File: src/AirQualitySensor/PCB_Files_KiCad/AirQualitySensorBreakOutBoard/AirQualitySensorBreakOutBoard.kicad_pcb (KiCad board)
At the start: 2 copper layers, 36 x 113.8 mm, 23 parts, among them J1 Conn_01x02_Male, J2 Conn_01x02_Male, J3 Conn_01x02_Male, J4 Conn_01x07_Male, Q1 IRLB8721PBF, U1 PMS5003, U2 PMS5003, U3 SPS30, U4 SHT31, U6 lilygo-ttgo-t-sim7000g-esp32-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, U7 Buck/Boost_Converter

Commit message: updated version
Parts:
- removed U7: Buck/Boost_Converter, Surfside Science:Buck_Boost_Converter
- added REF**: Buck_Boost_Converter, Surfside Science:Buck_Boost_Converter, F.Cu at (87.3, 38.8)
- moved ? 221.9 mm to (18.4, 17.9), turned to 90 degrees
- moved R4 210.4 mm to (25.6, 22.4), turned to 0 degrees
- moved R3 206.7 mm to (33.1, 19.6), turned to 180 degrees
- moved R2 206.4 mm to (18.6, 32.9), turned to 90 degrees
- moved U4 198.2 mm to (32.6, 27.8), turned to 0 degrees
- moved REF** 194.8 mm to (17.9, 45.9), turned to 90 degrees
- moved U1 194.8 mm to (26.8, 36.3), turned to 0 degrees
- moved U3 192.4 mm to (34.5, 31.5), turned to 180 degrees
- moved J4 187.9 mm to (55.1, 20.5), turned to -90 degrees
- moved C2 185.6 mm to (44.1, 29.9), turned to 0 degrees
- moved Q1 178.4 mm to (52.5, 30.2), turned to 0 degrees
- moved U2 169.9 mm to (54.9, 35.8), turned to 0 degrees
- moved J2 168.7 mm to (93.7, 18.9), turned to -90 degrees
- moved C1 167.1 mm to (67.6, 30.4), turned to 90 degrees
- moved U6 166.8 mm to (63.1, 33.1), turned to 90 degrees
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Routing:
- net PULLUP_1: track 70.8 -> 68.4 mm
- net GND: track 230.3 -> 232.0 mm
- net 3V3: track 144.4 -> 143.6 mm
- net VDD2: track 159.0 -> 159.7 mm
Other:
- board size 36 x 113.8 mm -> 113.8 x 36 mm

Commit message: Fixed bug aqs
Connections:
- U6 pad 12: unconnected-(U6-Pad12) -> VDD_EN
- U6 pad 13: VDD_EN -> unconnected-(U6-Pad13)
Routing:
- net VDD_EN: track 34.6 -> 31.9 mm
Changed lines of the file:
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@@
   (net 7 "unconnected-(U6-Pad03)")
   (net 8 "unconnected-(U6-Pad04)")
-  (net 9 "unconnected-(U6-Pad12)")
+  (net 9 "unconnected-(U6-Pad13)")
   (net 10 "unconnected-(U6-Pad14)")
   (net 11 "unconnected-(U6-Pad15)")
@@
       (net 34 "SPI_SS") (pinfunction "SPI__SS") (pintype "input"))
     (pad "12" thru_hole circle (at -14.12 -4.6 90) (size 2 2) (drill 1.02) (layers *.Cu *.Mask)
-      (net 9 "unconnected-(U6-Pad12)") (pinfunction "12") (pintype "input"))
+      (net 38 "VDD_EN") (pinfunction "12") (pintype "input"))
     (pad "13" thru_hole circle (at -14.12 -7.14 90) (size 2 2) (drill 1.02) (layers *.Cu *.Mask)
-      (net 38 "VDD_EN") (pinfunction "13") (pintype "input"))
+      (net 9 "unconnected-(U6-Pad13)") (pinfunction "13") (pintype "input"))
     (pad "14" thru_hole circle (at -14.12 -9.68 90) (size 2 2) (drill 1.02) (layers *.Cu *.Mask)
       (net 10 "unconnected-(U6-Pad14)") (pinfunction "14") (pintype "input"))
@@
   (segment (start 39.86 20.5) (end 38.085 18.725) (width 1) (layer "F.Cu") (net 37))
   (segment (start 38.085 18.725) (end 38.085 16.663353) (width 1) (layer "F.Cu") (net 37))
-  (segment (start 62.5 33.51) (end 62.5 33.6) (width 1) (layer "F.Cu") (net 38))
+  (segment (start 71.6 43.8) (end 70.174649 45.225351) (width 1) (layer "F.Cu") (net 38))
+  (segment (start 62.5 33.6) (end 65.6 36.7) (width 1) (layer "F.Cu") (net 38))
   (segment (start 71.6 38.8) (end 71.6 43.8) (width 1) (layer "F.Cu") (net 38))
-  (segment (start 69.5 36.7) (end 71.6 38.8) (width 1) (layer "F.Cu") (net 38))
-  (segment (start 70.174649 45.225351) (end 55.974649 45.225351) (width 1) (layer "F.Cu") (net 38))
   (segment (start 65.6 36.7) (end 69.5 36.7) (width 1) (layer "F.Cu") (net 38))
-  (segment (start 55.974649 45.225351) (end 55.974649 47.243002) (width 1) (layer "F.Cu") (net 38))
-  (segment (start 62.5 33.6) (end 65.6 36.7) (width 1) (layer "F.Cu") (net 38))
-  (segment (start 71.6 43.8) (end 70.174649 45.225351) (width 1) (layer "F.Cu") (net 38))
+  (segment (start 62.5 33.51) (end 62.5 33.6) (width 1) (layer "F.Cu") (net 38))
+  (segment (start 69.5 36.7) (end 71.6 38.8) (width 1) (layer "F.Cu") (net 38))
+  (segment (start 58.514649 45.485351) (end 58.514649 47.243002) (width 1) (layer "F.Cu") (net 38))
+  (segment (start 58.774649 45.225351) (end 58.514649 45.485351) (width 1) (layer "F.Cu") (net 38))
+  (segment (start 70.174649 45.225351) (end 58.774649 45.225351) (width 1) (layer "F.Cu") (net 38))
 )

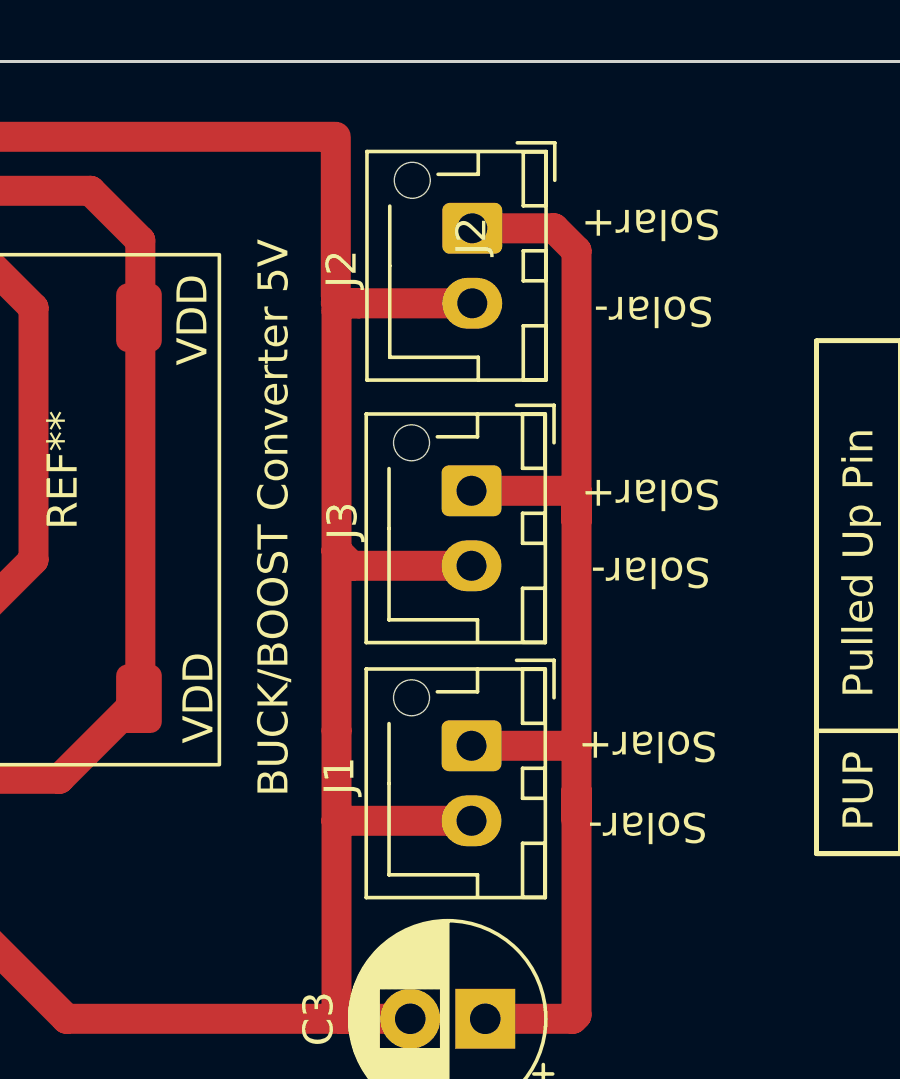
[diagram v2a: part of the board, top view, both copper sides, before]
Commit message: Updated AQS sensor code
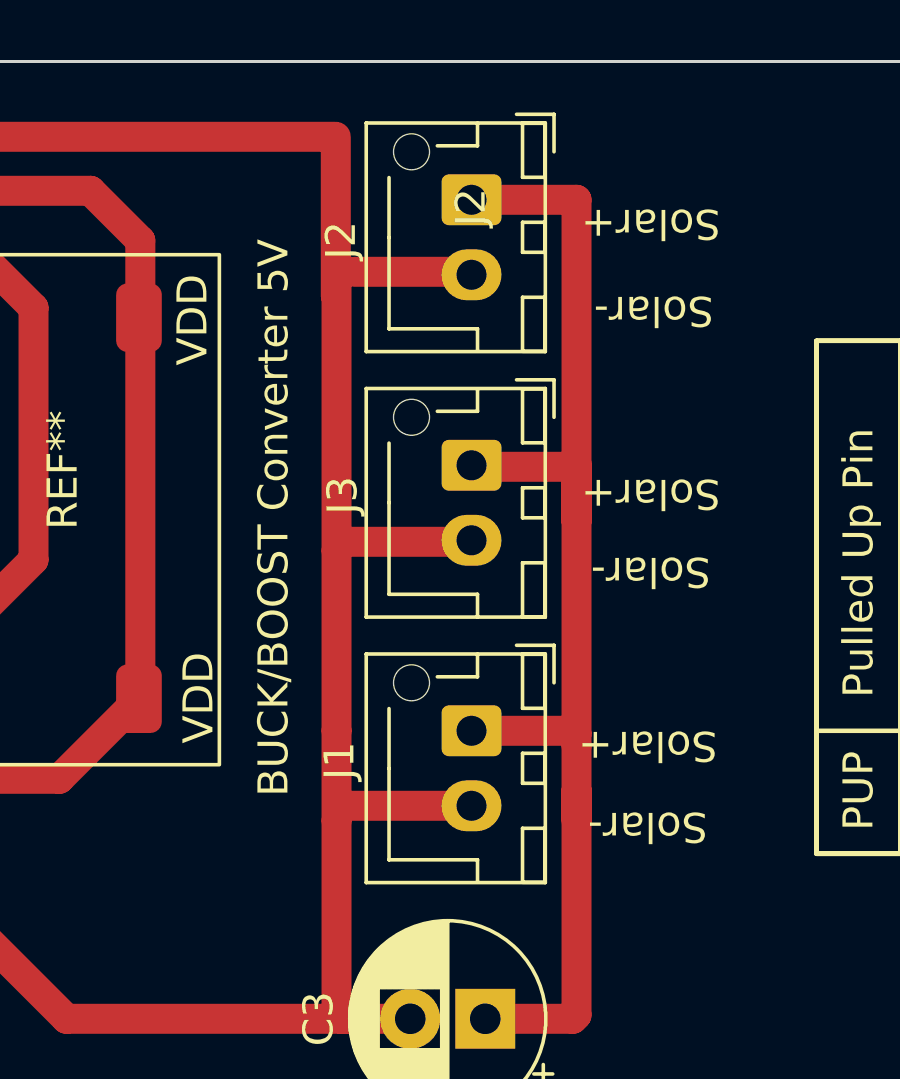
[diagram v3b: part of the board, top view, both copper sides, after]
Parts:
- moved J2 0.95 mm to (93.7, 18.0)
- moved J3 0.85 mm to (93.7, 26.9)
- moved J1 0.50 mm to (93.7, 35.7)
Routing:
- net Solar_IN: track 41.5 -> 43.6 mm
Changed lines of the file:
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@@
   (net 38 "VDD_EN")
   (footprint "Connector_JST:JST_XH_B2B-XH-AM_1x02_P2.50mm_Vertical" (layer "F.Cu")
-    (at 93.725 18.95 -90)
+    (at 93.7 18 -90)
     (descr "JST XH series connector, B2B-XH-AM, with boss (http://www.jst-mfg.com/product/pdf/eng/eXH.pdf), generated with kicad-footprint-generator")
     (tags "connector JST XH vertical boss")
@@
   )
   (footprint "Connector_JST:JST_XH_B2B-XH-AM_1x02_P2.50mm_Vertical" (layer "F.Cu")
-    (at 93.7 36.2 -90)
+    (at 93.7 35.7 -90)
     (descr "JST XH series connector, B2B-XH-AM, with boss (http://www.jst-mfg.com/product/pdf/eng/eXH.pdf), generated with kicad-footprint-generator")
     (tags "connector JST XH vertical boss")
@@
   )
   (footprint "Connector_JST:JST_XH_B2B-XH-AM_1x02_P2.50mm_Vertical" (layer "F.Cu")
-    (at 93.7 27.7 -90)
+    (at 93.7 26.85 -90)
     (descr "JST XH series connector, B2B-XH-AM, with boss (http://www.jst-mfg.com/product/pdf/eng/eXH.pdf), generated with kicad-footprint-generator")
     (tags "connector JST XH vertical boss")
@@
   (segment (start 57.357621 27.882379) (end 55.04 30.2) (width 1) (layer "F.Cu") (net 2))
   (segment (start 25.494649 47.243002) (end 27.537651 45.2) (width 1) (layer "F.Cu") (net 3))
+  (segment (start 93.65 29.4) (end 89.3 29.4) (width 1) (layer "F.Cu") (net 3))
   (segment (start 73.5 14.5) (end 74.9 15.9) (width 1) (layer "F.Cu") (net 3))
   (segment (start 69.4 38.4) (end 62.8 38.4) (width 1) (layer "F.Cu") (net 3))
   (segment (start 69.5 43.7) (end 70.2 43) (width 1) (layer "F.Cu") (net 3))
   (segment (start 44.9 43.7) (end 46.8 43.7) (width 1) (layer "F.Cu") (net 3))
-  (segment (start 93.7 38.7) (end 89.2 38.7) (width 1) (layer "F.Cu") (net 3))
+  (segment (start 93.7 38.35) (end 93.7 38.2) (width 1) (layer "F.Cu") (net 3))
   (segment (start 89.2 35.7) (end 89.2 29.7) (width 1) (layer "F.Cu") (net 3))
+  (segment (start 89.2 29.7) (end 89.2 20) (width 1) (layer "F.Cu") (net 3))
   (segment (start 89.2 38.7) (end 89.2 35.7) (width 1) (layer "F.Cu") (net 3))
-  (segment (start 93.7 30.2) (end 89.7 30.2) (width 1) (layer "F.Cu") (net 3))
   (segment (start 89.2 45.125) (end 89.2 38.7) (width 1) (layer "F.Cu") (net 3))
   (segment (start 46.8 43.7) (end 69.5 43.7) (width 1) (layer "F.Cu") (net 3))
+  (segment (start 89.8 20.4) (end 93.6 20.4) (width 1) (layer "F.Cu") (net 3))
   (segment (start 89.5 45.3) (end 80.2 45.3) (width 1) (layer "F.Cu") (net 3))
   (segment (start 27.537651 45.2) (end 43.4 45.2) (width 1) (layer "F.Cu") (net 3))
-  (segment (start 89.2 21.7) (end 89.45 21.45) (width 1) (layer "F.Cu") (net 3))
+  (segment (start 93.7 29.35) (end 93.65 29.4) (width 1) (layer "F.Cu") (net 3))
   (segment (start 46.617621 43.517621) (end 46.8 43.7) (width 1) (layer "F.Cu") (net 3))
   (segment (start 91.65738 45.3) (end 89.375 45.3) (width 1) (layer "F.Cu") (net 3))
@@
   (segment (start 58.394649 14.605351) (end 58.5 14.5) (width 1) (layer "F.Cu") (net 3))
   (segment (start 70.2 39.2) (end 69.4 38.4) (width 1) (layer "F.Cu") (net 3))
-  (segment (start 89.45 21.45) (end 89.95 21.45) (width 1) (layer "F.Cu") (net 3))
-  (segment (start 89.2 29.7) (end 89.2 21.7) (width 1) (layer "F.Cu") (net 3))
+  (segment (start 93.6 20.4) (end 93.7 20.5) (width 1) (layer "F.Cu") (net 3))
   (segment (start 66.8 35) (end 62 30.2) (width 1) (layer "F.Cu") (net 3))
-  (segment (start 89.95 21.45) (end 89.175 21.45) (width 1) (layer "F.Cu") (net 3))
   (segment (start 91.85738 45.2) (end 91.75738 45.3) (width 1) (layer "F.Cu") (net 3))
   (segment (start 70.2 43) (end 70.2 39.2) (width 1) (layer "F.Cu") (net 3))
   (segment (start 80.2 45.3) (end 69.9 35) (width 1) (layer "F.Cu") (net 3))
   (segment (start 69.9 35) (end 66.8 35) (width 1) (layer "F.Cu") (net 3))
-  (segment (start 89.7 30.2) (end 89.2 29.7) (width 1) (layer "F.Cu") (net 3))
   (segment (start 89.175 21.2) (end 89.175 15.9) (width 1) (layer "F.Cu") (net 3))
   (segment (start 58.394649 16.653002) (end 58.394649 14.605351) (width 1) (layer "F.Cu") (net 3))
-  (segment (start 93.792621 21.517621) (end 93.725 21.45) (width 1) (layer "F.Cu") (net 3))
   (segment (start 57.58 33.18) (end 57.58 30.2) (width 1) (layer "F.Cu") (net 3))
+  (segment (start 93.7 38.2) (end 89.3 38.2) (width 1) (layer "F.Cu") (net 3))
   (segment (start 74.9 15.9) (end 89.1 15.9) (width 1) (layer "F.Cu") (net 3))
   (segment (start 58.5 14.5) (end 73.5 14.5) (width 1) (layer "F.Cu") (net 3))
   (segment (start 91.75738 45.3) (end 91.65738 45.3) (width 1) (layer "F.Cu") (net 3))
-  (segment (start 89.95 21.45) (end 93.725 21.45) (width 1) (layer "F.Cu") (net 3))
   (segment (start 43.4 45.2) (end 44.9 43.7) (width 1) (layer "F.Cu") (net 3))
   (segment (start 30.454649 16.653002) (end 30.454649 14.5) (width 1) (layer "B.Cu") (net 3))
@@
   (segment (start 21.735 32.865) (end 19.5 35.1) (width 1) (layer "B.Cu") (net 32))
   (segment (start 22.894649 45.694649) (end 22.894649 47.263002) (width 1) (layer "B.Cu") (net 32))
-  (segment (start 97.2 28.7) (end 97.2 19.7) (width 1) (layer "F.Cu") (net 33))
-  (segment (start 97.2 27.7) (end 93.7 27.7) (width 1) (layer "F.Cu") (net 33))
+  (segment (start 97.1 26.9) (end 93.75 26.9) (width 1) (layer "F.Cu") (net 33))
+  (segment (start 97.1 35.7) (end 93.7 35.7) (width 1) (layer "F.Cu") (net 33))
+  (segment (start 97.2 18) (end 93.7 18) (width 1) (layer "F.Cu") (net 33))
+  (segment (start 97.2 35.8) (end 97.1 35.7) (width 1) (layer "F.Cu") (net 33))
+  (segment (start 97.2 28.7) (end 97.2 26.8) (width 1) (layer "F.Cu") (net 33))
   (segment (start 97.2 36.2) (end 97.2 28.7) (width 1) (layer "F.Cu") (net 33))
   (segment (start 97.2 37.7) (end 97.2 36.2) (width 1) (layer "F.Cu") (net 33))
   (segment (start 97.2 38.7) (end 97.2 37.7) (width 1) (layer "F.Cu") (net 33))
   (segment (start 97.075 45.3) (end 97.2 45.175) (width 1) (layer "F.Cu") (net 33))
-  (segment (start 96.45 18.95) (end 93.725 18.95) (width 1) (layer "F.Cu") (net 33))
-  (segment (start 97.2 36.2) (end 93.7 36.2) (width 1) (layer "F.Cu") (net 33))
-  (segment (start 97.2 19.7) (end 96.45 18.95) (width 1) (layer "F.Cu") (net 33))
-  (segment (start 97.2 28.7) (end 97.2 27.7) (width 1) (layer "F.Cu") (net 33))
+  (segment (start 97.2 28.7) (end 97.2 18) (width 1) (layer "F.Cu") (net 33))
   (segment (start 97.2 45.175) (end 97.2 37.7) (width 1) (layer "F.Cu") (net 33))
-  (segment (start 93.792621 19.017621) (end 93.725 18.95) (width 1) (layer "F.Cu") (net 33))
+  (segment (start 93.75 26.9) (end 93.7 26.85) (width 1) (layer "F.Cu") (net 33))
   (segment (start 94.15738 45.3) (end 97.075 45.3) (width 1) (layer "F.Cu") (net 33))
   (segment (start 45.694649 17.694649) (end 47.48 19.48) (width 1) (layer "F.Cu") (net 34))
